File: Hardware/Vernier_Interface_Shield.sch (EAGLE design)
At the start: 43 parts, among them U1 74HC4052SO, U2 LMV358SOICT

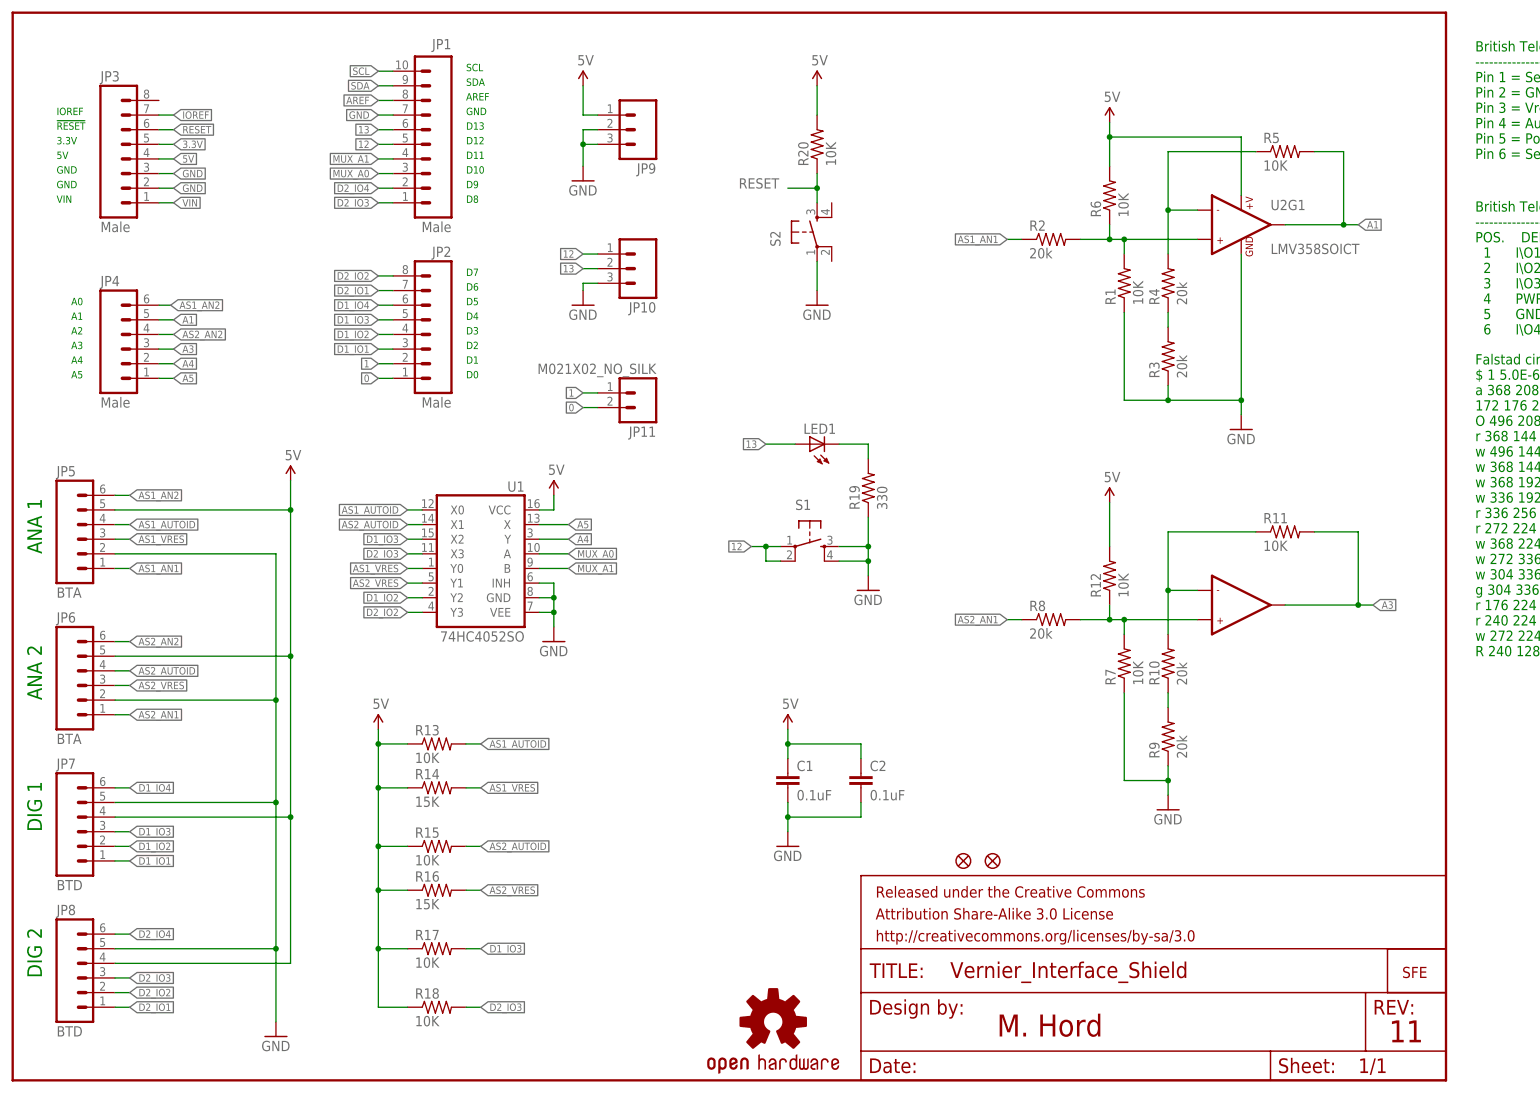
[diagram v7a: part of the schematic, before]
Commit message: Touched up schematic. Updated version number.
Pushed some schematic components onto grid. Replaced button symbols with
single action symbol.
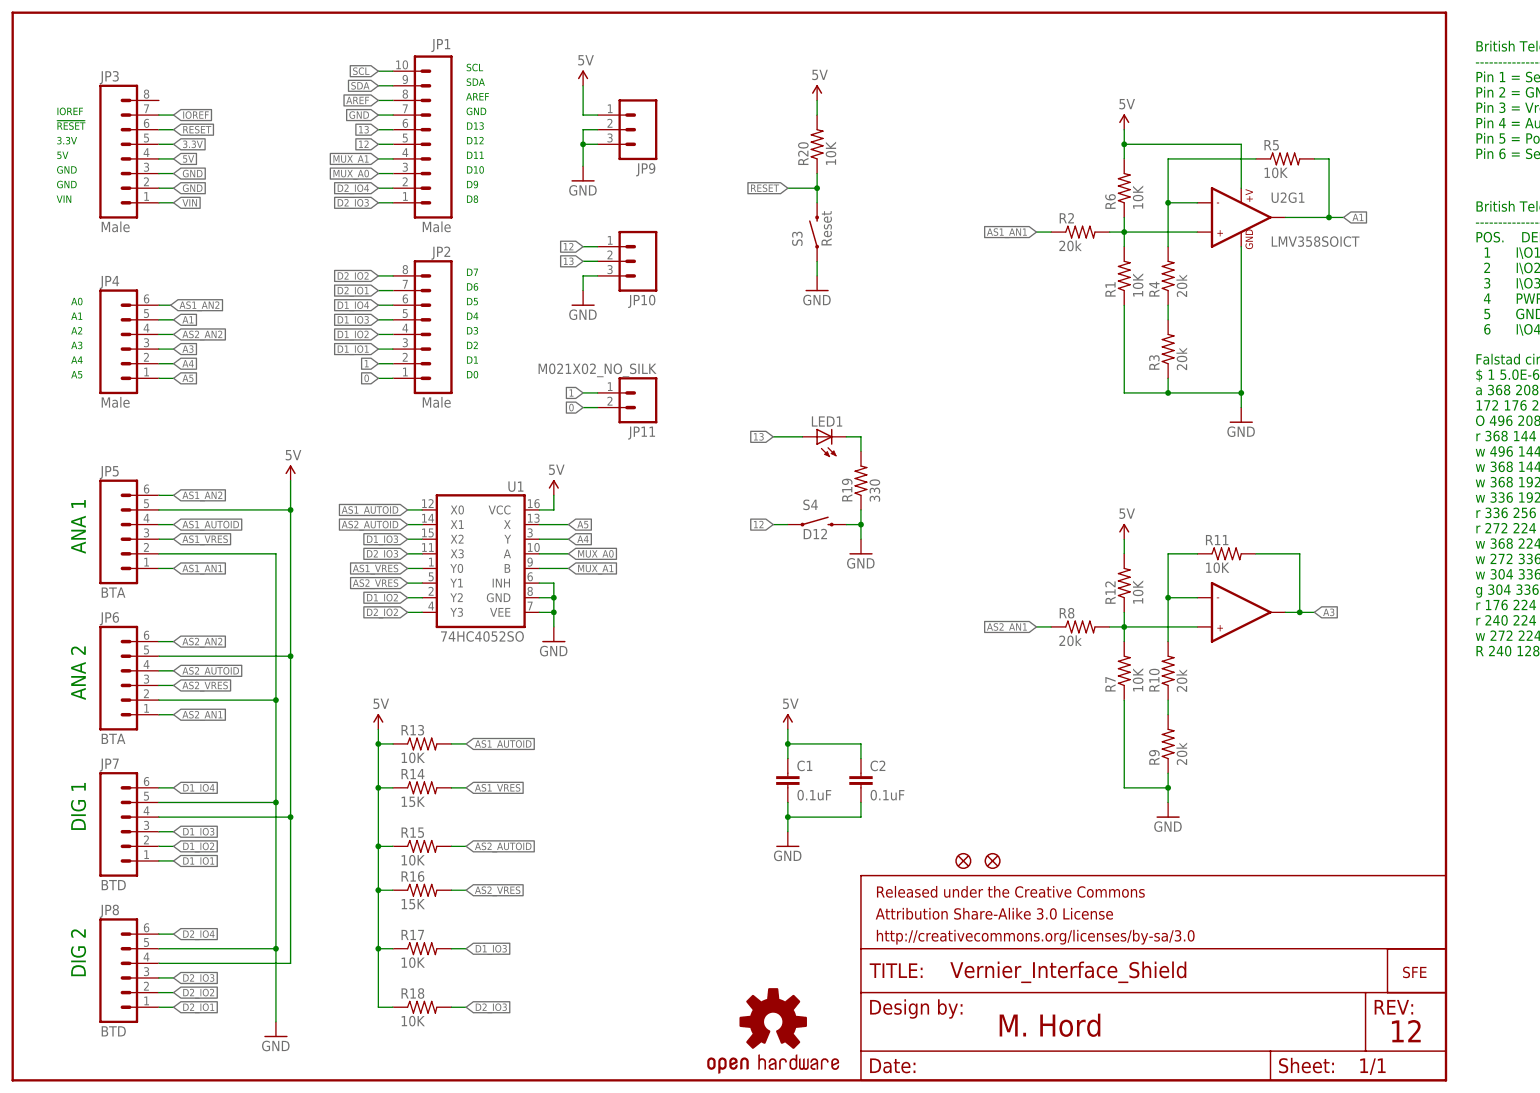
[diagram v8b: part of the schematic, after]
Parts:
- removed S1, S2: (no value), SparkFun-Electromechanical:TAC_SWITCHPTH
- added S3: Reset, SparkFun-Electromechanical:SWITCH-MOMENTARY-2PTH
- added S4: D12, SparkFun-Electromechanical:SWITCH-MOMENTARY-2PTH
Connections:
- net 12: now also S4.1; no longer S1.1, S1.2
- net GND: now also S3.1, S4.2; no longer S1.3, S1.4, S2.1
- net RESET: now also S3.2; no longer S2.3
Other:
- note added: "12"
- note removed: "11"
- moved on the sheet: JP10, JP5, JP6, JP7, JP8, LED1, R1, R10, R11, R12, R13, R14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
